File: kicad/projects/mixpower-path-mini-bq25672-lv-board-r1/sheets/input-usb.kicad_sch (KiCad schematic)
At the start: 29 parts, among them J1 USB_C_Receptacle_HRO_TYPE-C-3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, Q1 BSS138PS, U1 TL431DBZ, U2 TPD8S300A

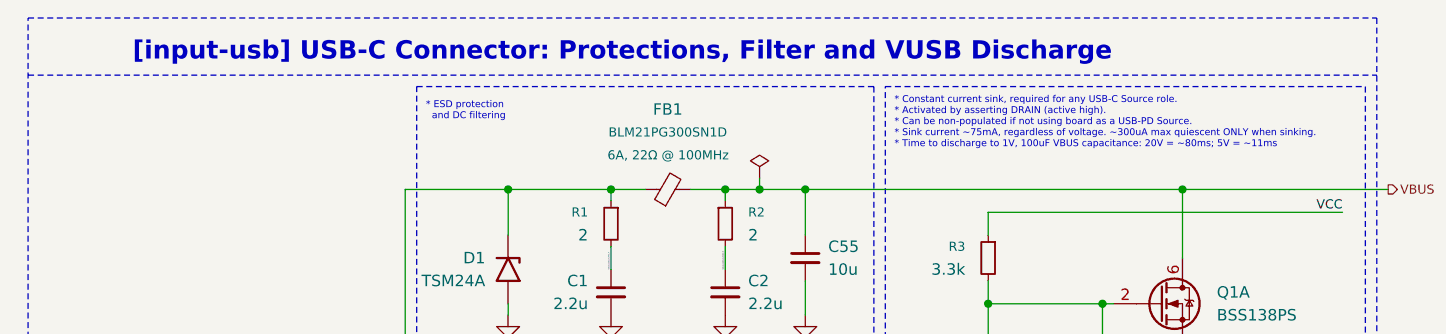
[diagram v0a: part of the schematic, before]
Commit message: feat: generate schematic PDF and fix minor schematic mistakes
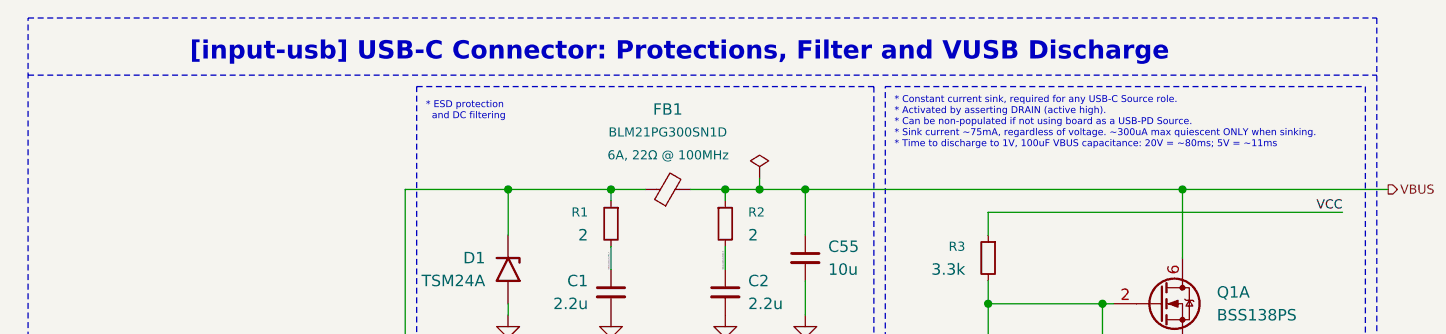
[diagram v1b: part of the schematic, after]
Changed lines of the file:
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@@
 	(text "[input-usb] USB-C Connector: Protections, Filter and VUSB Discharge"
 		(exclude_from_sim no)
-		(at 83.82 20.32 0)
+		(at 90.17 20.32 0)
 		(effects
 			(font

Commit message: feat: small changes in schematics, some PCB routing
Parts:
- R4, R6: footprint Resistor_SMD:R_0805_2012Metric -> Resistor_SMD:R_0402_1005Metric
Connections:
- net USBC_D+: now also J1.A6 (D+), J1.B6 (D+), R8.1, U2.16 (D4); no longer J1.A7 (D-), J1.B7 (D-), R7.1
- net USBC_D-: now also J1.A7 (D-), J1.B7 (D-), R7.1, U2.17 (D3); no longer J1.A6 (D+), J1.B6 (D+), R8.1
- no-connect marks 2 -> 0
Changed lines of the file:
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@@
 	(rectangle
 		(start 113.03 24.13)
-		(end 166.37 78.74)
+		(end 59.69 78.74)
 		(stroke
 			(width 0)
@@
 	)
 	(junction
+		(at 53.34 115.57)
+		(diameter 0)
+		(color 0 0 0 0)
+	)
+	(junction
+		(at 50.8 113.03)
+		(diameter 0)
+		(color 0 0 0 0)
+	)
+	(junction
 		(at 157.48 68.58)
 		(diameter 0)
@@
 		(color 0 0 0 0)
 	)
-	(no_connect
-		(at 62.23 120.65)
-	)
-	(no_connect
-		(at 62.23 118.11)
-	)
 	(wire
 		(pts
@@
 	(wire
 		(pts
-			(xy 53.34 113.03) (xy 53.34 90.17)
+			(xy 53.34 90.17) (xy 53.34 115.57)
 		)
 		(stroke
@@
 	(wire
 		(pts
-			(xy 62.23 115.57) (xy 50.8 115.57)
+			(xy 92.71 125.73) (xy 87.63 125.73)
 		)
 		(stroke
@@
 	(wire
 		(pts
-			(xy 92.71 125.73) (xy 87.63 125.73)
+			(xy 53.34 115.57) (xy 53.34 120.65)
 		)
 		(stroke
@@
 	(wire
 		(pts
+			(xy 50.8 113.03) (xy 62.23 113.03)
+		)
+		(stroke
+			(width 0)
+			(type default)
+		)
+	)
+	(wire
+		(pts
 			(xy 124.46 38.1) (xy 163.83 38.1)
 		)
@@
 	(wire
 		(pts
-			(xy 50.8 115.57) (xy 50.8 85.09)
+			(xy 50.8 85.09) (xy 50.8 113.03)
 		)
 		(stroke
@@
 	(wire
 		(pts
-			(xy 62.23 113.03) (xy 53.34 113.03)
+			(xy 50.8 113.03) (xy 50.8 118.11)
 		)
 		(stroke
@@
 	(wire
 		(pts
+			(xy 53.34 115.57) (xy 62.23 115.57)
+		)
+		(stroke
+			(width 0)
+			(type default)
+		)
+	)
+	(wire
+		(pts
 			(xy 57.15 110.49) (xy 57.15 127)
 		)
@@
 	(wire
 		(pts
+			(xy 62.23 120.65) (xy 53.34 120.65)
+		)
+		(stroke
+			(width 0)
+			(type default)
+		)
+	)
+	(wire
+		(pts
 			(xy 107.95 87.63) (xy 168.91 87.63)
 		)
@@
 	(wire
 		(pts
+			(xy 62.23 118.11) (xy 50.8 118.11)
+		)
+		(stroke
+			(width 0)
+			(type default)
+		)
+	)
+	(wire
+		(pts
 			(xy 93.98 91.44) (xy 93.98 93.98)
 		)
@@
 		)
 	)
-	(label "USBC_D-"
+	(label "USBC_D+"
 		(at 63.5 87.63 0)
 		(effects
@@
 		)
 	)
-	(label "USBC_D+"
+	(label "USBC_D-"
 		(at 63.5 82.55 0)
 		(effects
@@
 			)
 		)
-		(property "Footprint" "Resistor_SMD:R_0805_2012Metric"
+		(property "Footprint" "Resistor_SMD:R_0402_1005Metric"
 			(at 157.48 72.39 0)
 			(effects
@@
 		)
 		(instances
-			(project ""
+			(project "mixpower-path-mini-bq25672-lv-board-r1"
 				(path "/2e43857b-9bf9-460c-948c-ec2cf8a8d6b4/a96c4826-4f7b-4932-9621-9f42d0f49b09"
 					(reference "U2")
@@
 		)
 		(instances
-			(project ""
+			(project "mixpower-path-mini-bq25672-lv-board-r1"
 				(path "/2e43857b-9bf9-460c-948c-ec2cf8a8d6b4/a96c4826-4f7b-4932-9621-9f42d0f49b09"
 					(reference "FB1")
@@
 		)
 		(instances
-			(project ""
+			(project "mixpower-path-mini-bq25672-lv-board-r1"
 				(path "/2e43857b-9bf9-460c-948c-ec2cf8a8d6b4/a96c4826-4f7b-4932-9621-9f42d0f49b09"
 					(reference "Q1")
@@
 		)
 		(instances
-			(project ""
+			(project "mixpower-path-mini-bq25672-lv-board-r1"
 				(path "/2e43857b-9bf9-460c-948c-ec2cf8a8d6b4/a96c4826-4f7b-4932-9621-9f42d0f49b09"
 					(reference "Q1")
@@
 	)
 	(symbol
+		(lib_id "Reference_Voltage:TL431DBZ")
+		(at 137.16 54.61 270)
+		(mirror x)
+		(unit 1)
+		(exclude_from_sim no)
+		(in_bom yes)
+		(on_board yes)
+		(dnp no)
+		(fields_autoplaced yes)
+		(property "Reference" "U1"
+			(at 134.62 53.3399 90)
+			(effects
+				(font
+					(size 1.27 1.27)
+				)
+				(justify right)
+			)
+		)
+		(property "Value" "TL431DBZ"
+			(at 134.62 55.8799 90)
+			(effects
+				(font
+					(size 1.016 1.016)
+				)
+				(justify right)
+			)
+		)
+		(property "Footprint" "Package_TO_SOT_SMD:SOT-23"
+			(at 132.334 54.61 0)
+			(effects
+				(font
+					(size 1.27 1.27)
+					(italic yes)
+				)
+				(hide yes)
+			)
+		)
+		(property "Datasheet" "http://www.ti.com/lit/ds/symlink/tl431.pdf"
+			(at 128.016 52.832 0)
+			(effects
+				(font
+					(size 1.27 1.27)
+					(italic yes)
+				)
+				(hide yes)
+			)
+		)
+		(property "Description" "Shunt Regulator, SOT-23"
+			(at 130.048 54.61 0)
+			(effects
+				(font
+					(size 1.27 1.27)
+				)
+				(hide yes)
+			)
+		)
+		(pin "1"
+		)
+		(pin "2"
+		)
+		(pin "3"
+		)
+		(instances
+			(project "mixpower-path-mini-bq25672-lv-board-r1"
+				(path "/2e43857b-9bf9-460c-948c-ec2cf8a8d6b4/a96c4826-4f7b-4932-9621-9f42d0f49b09"
+					(reference "U1")
+					(unit 1)
+				)
+			)
+		)
+	)
+	(symbol
 		(lib_id "power:GND")
 		(at 157.48 74.93 0)
@@
 		)
 		(instances
-			(project ""
+			(project "mixpower-path-mini-bq25672-lv-board-r1"
 				(path "/2e43857b-9bf9-460c-948c-ec2cf8a8d6b4/a96c4826-4f7b-4932-9621-9f42d0f49b09"
 					(reference "TP1")
@@
 			)
 		)
-		(property "Footprint" "Resistor_SMD:R_0805_2012Metric"
+		(property "Footprint" "Resistor_SMD:R_0402_1005Metric"
 			(at 124.46 55.88 0)
 			(effects
@@
 	)
 	(symbol
-		(lib_id "Reference_Voltage:TL431DBZ")
-		(at 137.16 54.61 270)
-		(mirror x)
-		(unit 1)
-		(exclude_from_sim no)
-		(in_bom yes)
-		(on_board yes)
-		(dnp no)
-		(property "Reference" "U1"
-			(at 135.89 54.6099 90)
-			(effects
-				(font
-					(size 1.27 1.27)
-				)
-				(justify right)
-			)
-		)
-		(property "Value" "TL431DBZ"
-			(at 135.89 57.1499 90)
-			(effects
-				(font
-					(size 1.016 1.016)
-				)
-				(justify right)
-			)
-		)
-		(property "Footprint" "Package_TO_SOT_SMD:SOT-23"
-			(at 132.334 54.61 0)
-			(effects
-				(font
-					(size 1.27 1.27)
-					(italic yes)
-				)
-				(hide yes)
-			)
-		)
-		(property "Datasheet" "http://www.ti.com/lit/ds/symlink/tl431.pdf"
-			(at 128.016 52.832 0)
-			(effects
-				(font
-					(size 1.27 1.27)
-					(italic yes)
-				)
-				(hide yes)
-			)
-		)
-		(property "Description" "Shunt Regulator, SOT-23"
-			(at 130.048 54.61 0)
-			(effects
-				(font
-					(size 1.27 1.27)
-				)
-				(hide yes)
-			)
-		)
-		(pin "1"
-		)
-		(pin "2"
-		)
-		(pin "3"
-		)
-		(instances
-			(project ""
-				(path "/2e43857b-9bf9-460c-948c-ec2cf8a8d6b4/a96c4826-4f7b-4932-9621-9f42d0f49b09"
-					(reference "U1")
-					(unit 1)
-				)
-			)
-		)
-	)
-	(symbol
 		(lib_id "power:PWR_FLAG")
 		(at 30.48 130.81 0)
@@
 		)
 		(instances
-			(project ""
+			(project "mixpower-path-mini-bq25672-lv-board-r1"
 				(path "/2e43857b-9bf9-460c-948c-ec2cf8a8d6b4/a96c4826-4f7b-4932-9621-9f42d0f49b09"
 					(reference "#FLG02")
@@
 		)
 		(instances
-			(project ""
+			(project "mixpower-path-mini-bq25672-lv-board-r1"
 				(path "/2e43857b-9bf9-460c-948c-ec2cf8a8d6b4/a96c4826-4f7b-4932-9621-9f42d0f49b09"
 					(reference "TP4")
@@
 		)
 		(instances
-			(project ""
+			(project "mixpower-path-mini-bq25672-lv-board-r1"
 				(path "/2e43857b-9bf9-460c-948c-ec2cf8a8d6b4/a96c4826-4f7b-4932-9621-9f42d0f49b09"
 					(reference "C6")

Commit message: feat: failed PCB routing
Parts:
- removed C55: 10u, Capacitor_SMD:C_0402_1005Metric, symbol Device:C_Small
- removed D1: TSM24A, Package_TO_SOT_SMD:SOT-23, symbol Diode:TSM24A
- removed Q1: BSS138PS, mixlib-generic-sot:SOT-363_SC-70-6, symbol mixlib-discrete-mosfet:BSS138PS
- removed R3: 3.3k, Resistor_SMD:R_0402_1005Metric, symbol Device:R_Small
- removed R4: 10M, Resistor_SMD:R_0402_1005Metric, symbol Device:R_Small
- removed U1: TL431DBZ, Package_TO_SOT_SMD:SOT-23, symbol Reference_Voltage:TL431DBZ
- added C5: 10u, Capacitor_SMD:C_0402_1005Metric, symbol Device:C_Small
- added D1: PESD24VV1BA, Diode_SMD:D_SOD-323, symbol Device:D_TVS_Small
- added Q1: DMG1029SVQ, mixlib-generic-sot:SOT-563, symbol mixlib-discrete-mosfet:DMG1029SVQ
- added R10, R7: 220, Resistor_SMD:R_0402_1005Metric, symbol Device:R_Small
- added R8: 1M, Resistor_SMD:R_0402_1005Metric, symbol Device:R_Small
- C2: renamed from C1; value 2.2u -> 10n
- C4: renamed from C2; value 2.2u -> 100n
- R3: renamed from R7; value 22 -> 27
- R4: renamed from R8; value 22 -> 27
- R9: renamed from R5; value 33 -> 1.2k; footprint Resistor_SMD:R_0805_2012Metric -> Resistor_SMD:R_1210_3225Metric
- renumbered C3 to C1, C6 to C3, C4 to C6, C5 to C7, R9 to R1, R6 to R11, R10 to R2, R1 to R5, R2 to R6, TP4 to TP1, TP5 to TP2, TP6 to TP3, TP7 to TP4, TP1 to TP5, U2 to U1
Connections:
- net DISCH: now also R10.2
- net GND: now also C5.2, D1.1 (A1), Q1.1 (S1), R8.2
- net VBUS: now also R9.1, C5.1
- net VBUS_USBC_IN: now also D1.2 (A2)
- net VCC: now also Q1.4 (S2); no longer C1.1, U1.10 (VPWR)
- net DISCH_DRAIN: now reaches R9.2
- net DISCH_DRAIN: now also Q1.6 (D1)
- new net: Q1.5 (G2), R7.2
- new net DISCH_G: Q1.2 (G1), R10.1
- new net USBC_TPS_VCC: C1.1, Q1.3 (D2), U1.10 (VPWR)
- new net VCC_DIS: R7.1, R8.1
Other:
- note added: "* Current sink, required for any USB-C Source role. * Activated by asserting DISCH (active high). * Can be non-populated if not using board as a USB-PD Source. * Time to discharge to 1V, 100uF VBUS capacitance: 24V = ~294ms; 5V = ~200ms"
- note added: "* ESD protection and DC filtering. * Not sure how much attention must be given to proper pi-filter calculations. I suppose some filtering is enough."
- note added: "* Place close to TPD."
- note added: "* This cuts power for the TPD chip (default: powered). CC1/CC2 will be disconnected when unpowered. * Three possibilities. (1) If the board is battery-powered or externally powered, and USB-C is not connected, dead-battery support is not needed, so the TPD doesn't need to be powered. (2) If the board is not powered or in a dead-battery situation (e.g. ship mode), and USB-C is connected, TPD will 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"
- note removed: "* Constant current sink, required for any USB-C Source role. * Activated by asserting DRAIN (active high). * Can be non-populated if not using board as a USB-PD Source. * Sink current ~75mA, regardless of voltage. ~300uA max quiescent ONLY when sinking. * Time to discharge to 1V, 100uF VBUS capacitance: 20V = ~80ms; 5V = ~11ms"
- note removed: "* ESD protection and DC filtering"
- moved on the sheet: C1, C2, C3, C4, C6, C7, FB1, JP1, R1, R11, R2, R3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
